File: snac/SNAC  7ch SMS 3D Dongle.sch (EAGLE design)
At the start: 14 parts, among them IC1 MAX660CPACS, IC2 4030D, K2 692112030100, Q9 BC849SMD, X2 STEREOJACK

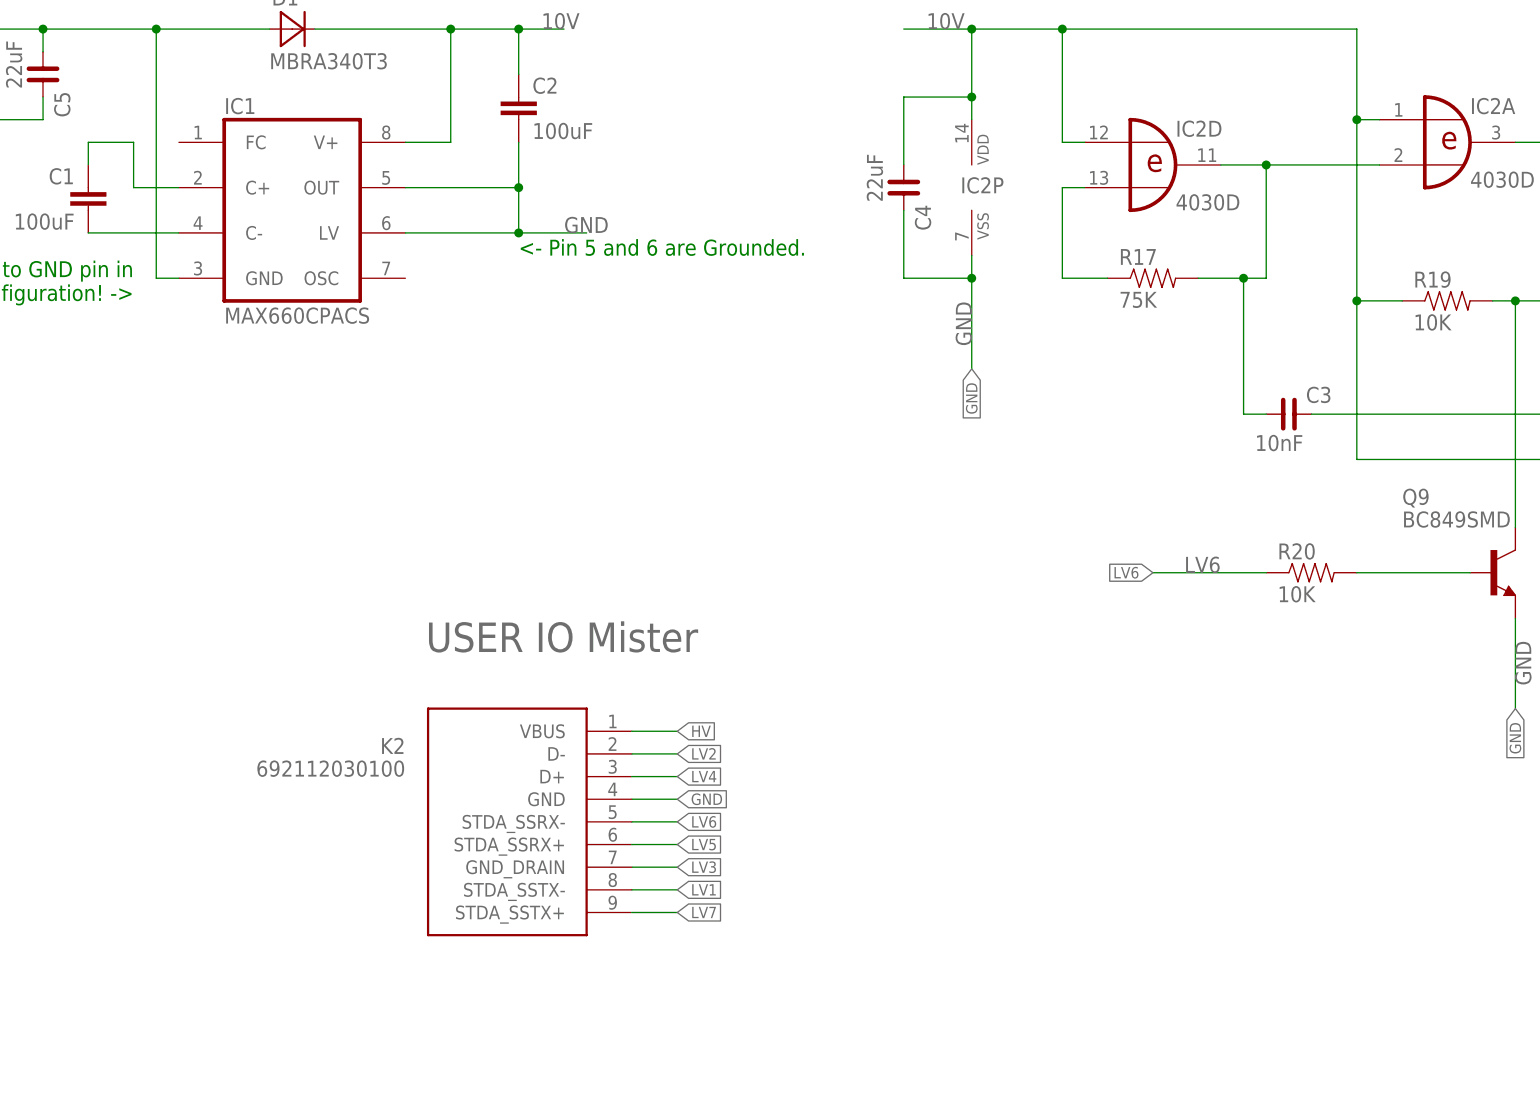
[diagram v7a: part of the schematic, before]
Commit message: XOR Osc on 3D boards needed an extra resistor
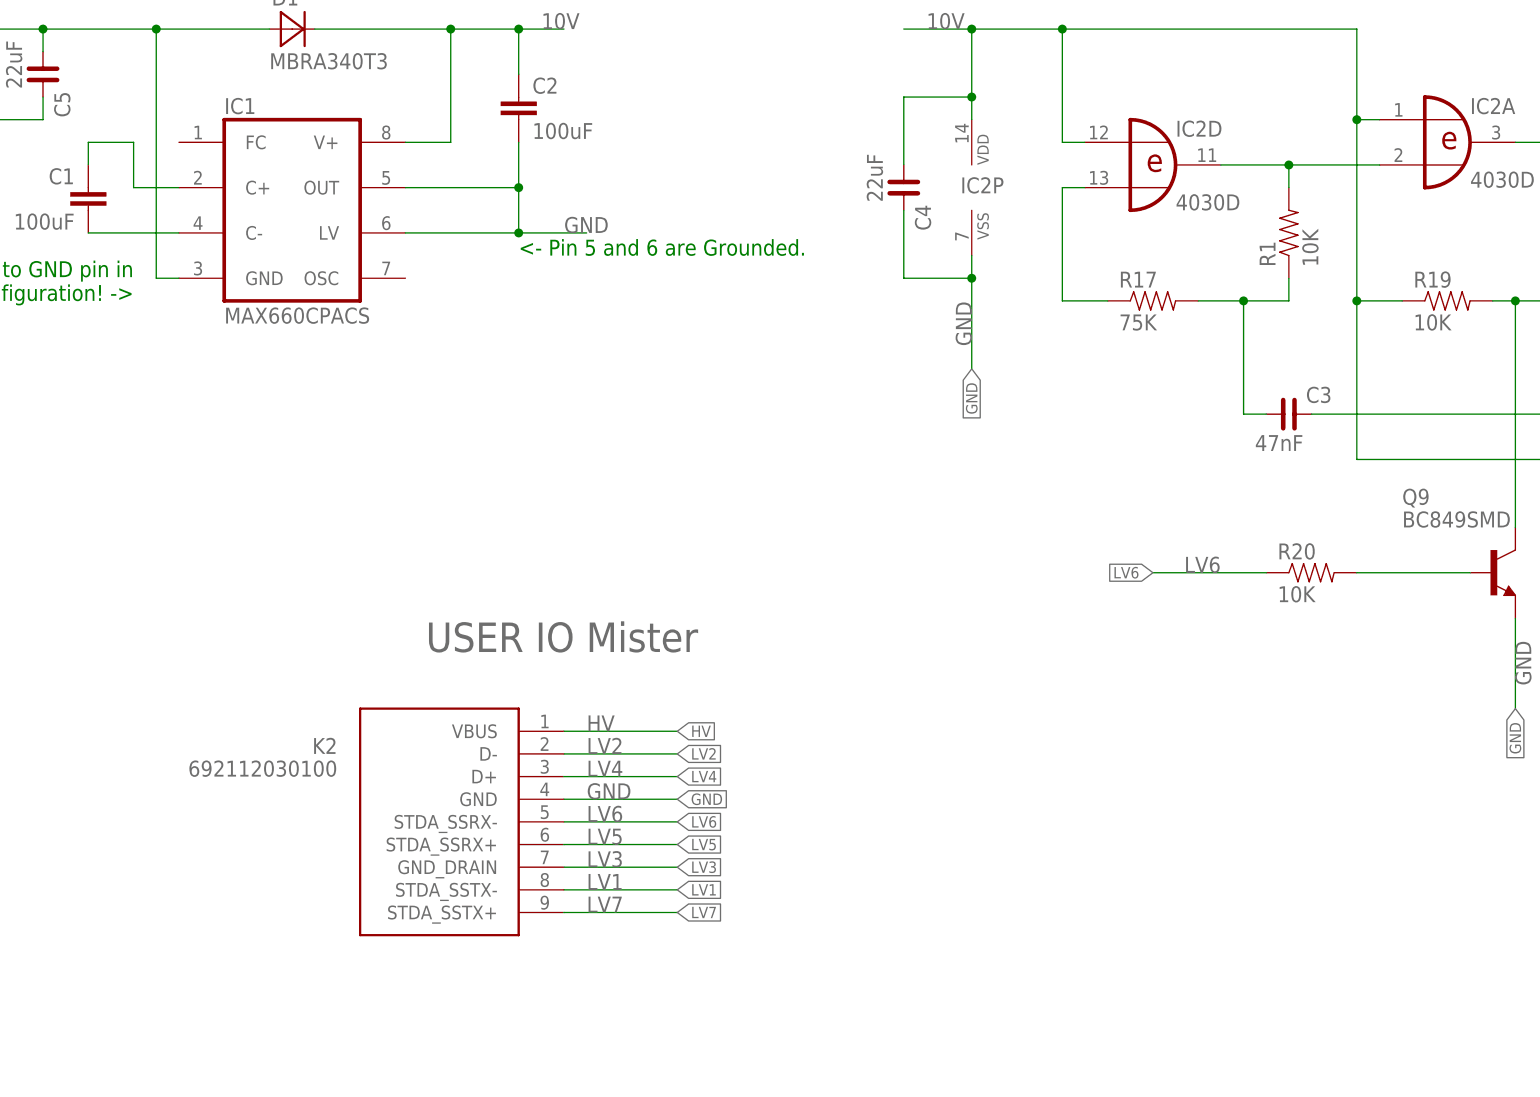
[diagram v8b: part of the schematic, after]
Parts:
- added R1: 10K, SparkFun:RESISTOR0603-RES
- C3: value 10nF -> 47nF
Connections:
- new net N$6: IC2A.I1, IC2D.O, R1.2
- net N$5: now also R1.1; no longer IC2A.I1, IC2D.O
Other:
- moved on the sheet: K2, R17
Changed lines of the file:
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@@
 <part name="IC2" library="40xx" deviceset="4030" device="D"/>
 <part name="R17" library="SparkFun" deviceset="RESISTOR" device="0603-RES" value="75K"/>
-<part name="C3" library="rc-master-smd" deviceset="C_" device="0805" value="10nF"/>
+<part name="C3" library="rc-master-smd" deviceset="C_" device="0805" value="47nF"/>
 <part name="Q9" library="transistor-npn" library_urn="urn:adsk.eagle:library:398" deviceset="BC849*" device="SMD" package3d_urn="urn:adsk.eagle:package:28748/2"/>
 <part name="R19" library="SparkFun" deviceset="RESISTOR" device="0603-RES" value="10K"/>
@@
 <part name="C2" library="rcl" library_urn="urn:adsk.eagle:library:334" deviceset="C-EU" device="C1210" package3d_urn="urn:adsk.eagle:package:23619/2" value="100uF"/>
 <part name="C1" library="rcl" library_urn="urn:adsk.eagle:library:334" deviceset="C-EU" device="C1210" package3d_urn="urn:adsk.eagle:package:23619/2" value="100uF"/>
+<part name="R1" library="SparkFun" deviceset="RESISTOR" device="0603-RES" value="10K"/>
 </parts>
 <sheets>
@@
 <instance part="FRAME1" gate="G$1" x="0" y="40.64"/>
 <instance part="FRAME1" gate="G$2" x="147.32" y="40.64"/>
-<instance part="K2" gate="G$1" x="91.44" y="116.84" rot="MR0"/>
+<instance part="K2" gate="G$1" x="83.82" y="116.84" rot="MR0"/>
 <instance part="IC2" gate="A" x="195.58" y="187.96"/>
 <instance part="IC2" gate="B" x="223.52" y="172.72"/>
 <instance part="IC2" gate="C" x="223.52" y="154.94"/>
 <instance part="IC2" gate="D" x="162.56" y="185.42"/>
-<instance part="R17" gate="G$1" x="162.56" y="172.72"/>
+<instance part="R17" gate="G$1" x="162.56" y="170.18"/>
 <instance part="C3" gate="G$1" x="177.8" y="157.48"/>
 <instance part="Q9" gate="G$1" x="200.66" y="139.7"/>
@@
 <instance part="C2" gate="G$1" x="91.44" y="193.04"/>
 <instance part="C1" gate="G$1" x="43.18" y="182.88" rot="MR0"/>
+<instance part="R1" gate="G$1" x="177.8" y="177.8" rot="R90"/>
 </instances>
 <busses>
@@
 <segment>
 <pinref part="K2" gate="G$1" pin="VBUS"/>
-<wire x1="104.14" y1="121.92" x2="109.22" y2="121.92" width="0.1524" layer="91"/>
+<wire x1="96.52" y1="121.92" x2="109.22" y2="121.92" width="0.1524" layer="91"/>
 <label x="109.22" y="121.92" size="1.27" layer="95" xref="yes"/>
+<label x="99.06" y="121.92" size="1.778" layer="95"/>
 </segment>
 <segment>
@@
 <segment>
 <pinref part="K2" gate="G$1" pin="D-"/>
-<wire x1="104.14" y1="119.38" x2="109.22" y2="119.38" width="0.1524" layer="91"/>
+<wire x1="96.52" y1="119.38" x2="109.22" y2="119.38" width="0.1524" layer="91"/>
 <label x="109.22" y="119.38" size="1.27" layer="95" xref="yes"/>
+<label x="99.06" y="119.38" size="1.778" layer="95"/>
 </segment>
 </net>
@@
 <segment>
 <pinref part="K2" gate="G$1" pin="STDA_SSTX-"/>
-<wire x1="104.14" y1="104.14" x2="109.22" y2="104.14" width="0.1524" layer="91"/>
+<wire x1="96.52" y1="104.14" x2="109.22" y2="104.14" width="0.1524" layer="91"/>
 <label x="109.22" y="104.14" size="1.27" layer="95" xref="yes"/>
+<label x="99.06" y="104.14" size="1.778" layer="95"/>
 </segment>
 </net>
@@
 <segment>
 <pinref part="K2" gate="G$1" pin="D+"/>
-<wire x1="104.14" y1="116.84" x2="109.22" y2="116.84" width="0.1524" layer="91"/>
+<wire x1="96.52" y1="116.84" x2="109.22" y2="116.84" width="0.1524" layer="91"/>
 <label x="109.22" y="116.84" size="1.27" layer="95" xref="yes"/>
+<label x="99.06" y="116.84" size="1.778" layer="95"/>
 </segment>
 </net>
@@
 <segment>
 <pinref part="K2" gate="G$1" pin="GND_DRAIN"/>
-<wire x1="104.14" y1="106.68" x2="109.22" y2="106.68" width="0.1524" layer="91"/>
+<wire x1="96.52" y1="106.68" x2="109.22" y2="106.68" width="0.1524" layer="91"/>
 <label x="109.22" y="106.68" size="1.27" layer="95" xref="yes"/>
+<label x="99.06" y="106.68" size="1.778" layer="95"/>
 </segment>
 </net>
@@
 <segment>
 <pinref part="K2" gate="G$1" pin="STDA_SSRX+"/>
-<wire x1="104.14" y1="109.22" x2="109.22" y2="109.22" width="0.1524" layer="91"/>
+<wire x1="96.52" y1="109.22" x2="109.22" y2="109.22" width="0.1524" layer="91"/>
 <label x="109.22" y="109.22" size="1.27" layer="95" xref="yes"/>
+<label x="99.06" y="109.22" size="1.778" layer="95"/>
 </segment>
 </net>
@@
 <segment>
 <pinref part="K2" gate="G$1" pin="STDA_SSRX-"/>
-<wire x1="104.14" y1="111.76" x2="109.22" y2="111.76" width="0.1524" layer="91"/>
+<wire x1="96.52" y1="111.76" x2="109.22" y2="111.76" width="0.1524" layer="91"/>
 <label x="109.22" y="111.76" size="1.27" layer="95" xref="yes"/>
 <label x="162.56" y="139.7" size="1.27" layer="95" rot="MR0" xref="yes"/>
+<label x="99.06" y="111.76" size="1.778" layer="95"/>
 </segment>
 <segment>
@@
 <segment>
 <pinref part="K2" gate="G$1" pin="STDA_SSTX+"/>
-<wire x1="104.14" y1="101.6" x2="109.22" y2="101.6" width="0.1524" layer="91"/>
+<wire x1="96.52" y1="101.6" x2="109.22" y2="101.6" width="0.1524" layer="91"/>
 <label x="109.22" y="101.6" size="1.27" layer="95" xref="yes"/>
+<label x="99.06" y="101.6" size="1.778" layer="95"/>
 </segment>
 </net>
@@
 <segment>
 <pinref part="K2" gate="G$1" pin="GND"/>
-<wire x1="104.14" y1="114.3" x2="109.22" y2="114.3" width="0.1524" layer="91"/>
+<wire x1="96.52" y1="114.3" x2="109.22" y2="114.3" width="0.1524" layer="91"/>
 <label x="109.22" y="114.3" size="1.27" layer="95" xref="yes"/>
 <label x="203.2" y="124.46" size="1.27" layer="95" rot="R270" xref="yes"/>
 <label x="142.24" y="162.56" size="1.27" layer="95" rot="R270" xref="yes"/>
+<label x="99.06" y="114.3" size="1.778" layer="95"/>
 </segment>
 <segment>
@@
 <net name="N$5" class="0">
 <segment>
-<pinref part="IC2" gate="D" pin="O"/>
-<pinref part="IC2" gate="A" pin="I1"/>
-<wire x1="170.18" y1="185.42" x2="175.26" y2="185.42" width="0.1524" layer="91"/>
 <pinref part="R17" gate="G$1" pin="2"/>
-<wire x1="175.26" y1="185.42" x2="187.96" y2="185.42" width="0.1524" layer="91"/>
-<wire x1="167.64" y1="172.72" x2="172.72" y2="172.72" width="0.1524" layer="91"/>
-<wire x1="172.72" y1="172.72" x2="175.26" y2="172.72" width="0.1524" layer="91"/>
-<wire x1="175.26" y1="172.72" x2="175.26" y2="185.42" width="0.1524" layer="91"/>
-<junction x="175.26" y="185.42"/>
+<wire x1="167.64" y1="170.18" x2="172.72" y2="170.18" width="0.1524" layer="91"/>
 <pinref part="C3" gate="G$1" pin="1"/>
 <wire x1="175.26" y1="157.48" x2="172.72" y2="157.48" width="0.1524" layer="91"/>
-<wire x1="172.72" y1="157.48" x2="172.72" y2="172.72" width="0.1524" layer="91"/>
-<junction x="172.72" y="172.72"/>
+<wire x1="172.72" y1="157.48" x2="172.72" y2="170.18" width="0.1524" layer="91"/>
+<junction x="172.72" y="170.18"/>
+<pinref part="R1" gate="G$1" pin="1"/>
+<wire x1="172.72" y1="170.18" x2="177.8" y2="170.18" width="0.1524" layer="91"/>
+<wire x1="177.8" y1="170.18" x2="177.8" y2="172.72" width="0.1524" layer="91"/>
 </segment>
 </net>
@@
 <pinref part="R17" gate="G$1" pin="1"/>
 <wire x1="152.4" y1="182.88" x2="154.94" y2="182.88" width="0.1524" layer="91"/>
-<wire x1="157.48" y1="172.72" x2="152.4" y2="172.72" width="0.1524" layer="91"/>
-<wire x1="152.4" y1="172.72" x2="152.4" y2="182.88" width="0.1524" layer="91"/>
+<wire x1="157.48" y1="170.18" x2="152.4" y2="170.18" width="0.1524" layer="91"/>
+<wire x1="152.4" y1="170.18" x2="152.4" y2="182.88" width="0.1524" layer="91"/>
 </segment>
 </net>
@@
 </segment>
 </net>
+<net name="N$6" class="0">
+<segment>
+<pinref part="IC2" gate="A" pin="I1"/>
+<pinref part="IC2" gate="D" pin="O"/>
+<wire x1="170.18" y1="185.42" x2="177.8" y2="185.42" width="0.1524" layer="91"/>
+<pinref part="R1" gate="G$1" pin="2"/>
+<wire x1="177.8" y1="185.42" x2="187.96" y2="185.42" width="0.1524" layer="91"/>
+<wire x1="177.8" y1="182.88" x2="177.8" y2="185.42" width="0.1524" layer="91"/>
+<junction x="177.8" y="185.42"/>
+</segment>
+</net>
 </nets>
 </sheet>
 </sheets>
+<errors>
+</errors>
 </schematic>
 </drawing>
